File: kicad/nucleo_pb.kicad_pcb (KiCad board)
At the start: 2 copper layers, 91.4 x 91.4 mm, 273 parts, among them CN10 2X19_HEADER, CN7 2X19_HEADER, P1 CONN_2, P10 CONN_2, P11 CONN_2, P12 CONN_2, P13 CONN_2, P14 CONN_2, P15 CONN_2, P16 CONN_2, P17 CONN_2, P18 CONN_2, P19 CONN_2, P2 CONN_2, P20 CONN_2, P21 CONN_2, P22 CONN_2, P23 CONN_2, P24 CONN_2, P25 CONN_2, P26 CONN_2, P27 CONN_2, P28 CONN_2, P29 CONN_2, P3 CONN_2, P30 CONN_2, P31 CONN_2, P32 CONN_2, P33 CONN_2, P34 CONN_2, P35 CONN_2, P36 CONN_2, P37 CONN_2, P38 CONN_2, P39 CONN_2, P4 CONN_2, P40 CONN_2, P41 CONN_2, P42 CONN_2, P43 CONN_2, P44 CONN_2, P45 CONN_2, P46 CONN_2, P47 CONN_2, P48 CONN_2, P49 CONN_2, P5 CONN_2, P50 CONN_2, P51 CONN_2, P52 CONN_2, P53 CONN_2, P54 CONN_2, P55 CONN_2, P56 CONN_2, P57 CONN_2, P58 CONN_2, P59 CONN_2, P6 CONN_2, P60 CONN_2, P61 CONN_2, P62 CONN_2, P63 CONN_2, P64 CONN_2, P65 CONN_2, P66 CONN_2, P67 CONN_2, P68 CONN_2, P69 CONN_2, P7 CONN_2, P70 CONN_2, P71 CONN_2, P72 CONN_2, P73 CONN_2, P74 CONN_2, P75 CONN_2, P76 CONN_2, P77 SOIC_AREA, P8 CONN_2, P9 CONN_2, U1 TSSOP28_BREAKOUT

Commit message: added power rails
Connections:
- PROTO_1PIN pad 10: (no net) -> /5V (x2)
- PROTO_1PIN pad 10: (no net) -> /3V3 (x11)
- PROTO_1PIN pad 10: (no net) -> /GND (x8)
- PROTO_AREA pad 1: (no net) -> /5V (x2)
- PROTO_AREA pad 7: (no net) -> /5V (x2)
- PROTO_AREA pad 8: (no net) -> /5V (x2)
- PROTO_AREA pad 3: (no net) -> /3V3
- PROTO_AREA pad 4: (no net) -> /3V3
- PROTO_AREA pad 5: (no net) -> /3V3
- PROTO_AREA pad 1: (no net) -> /GND (x2)
- PROTO_AREA pad 2: (no net) -> /5V (x2)
- PROTO_AREA pad 6: (no net) -> /5V (x2)
- PROTO_AREA pad 7: (no net) -> /GND (x2)
- PROTO_AREA pad 8: (no net) -> /GND (x2)
- PROTO_AREA pad 9: (no net) -> /5V (x2)
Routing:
- net /3V3: track 10.8 -> 89.7 mm
- net /5V: track 10.8 -> 84.9 mm
- net /GND: track 69.8 -> 138.8 mm
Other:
- board text added: "CC BY 4.0 aon@umetronics.com 2015"
- board text added: "G"
- board text added: "STM32 Nucleo Prototyping Shield v1.2"
- board text removed: "CC-BY aon@umetronics.com 2015"
- board text removed: "STM32 Nucleo Prototyping Shield v1.1"

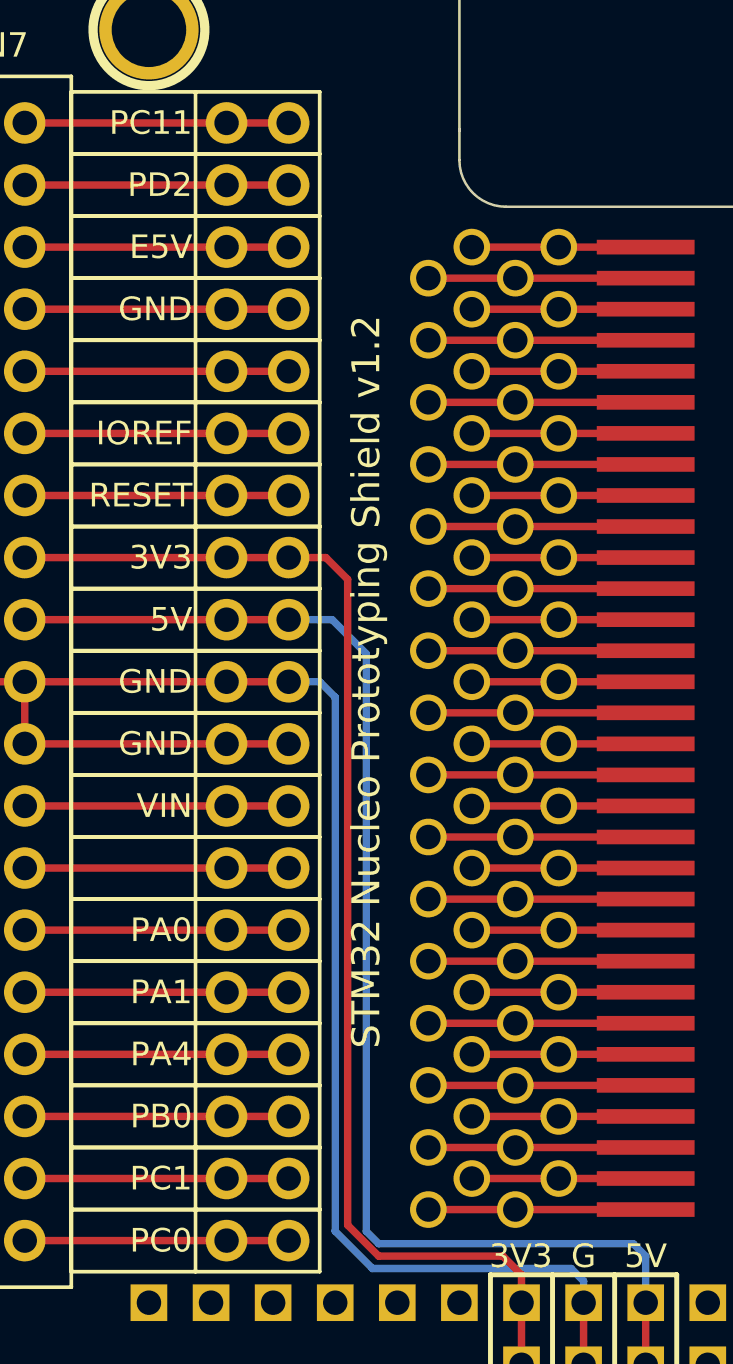
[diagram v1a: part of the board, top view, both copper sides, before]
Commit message: nucleo-64 silkscreen text
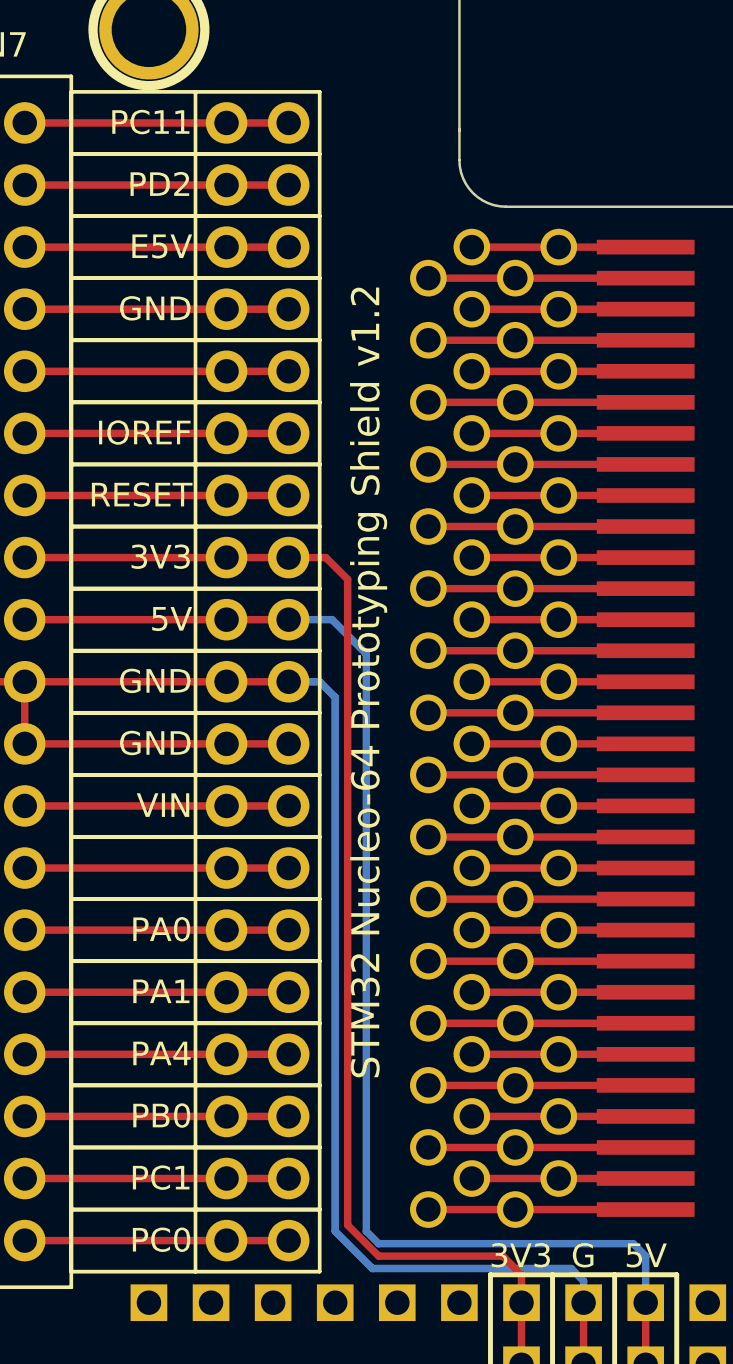
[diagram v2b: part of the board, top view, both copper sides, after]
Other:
- board text added: "STM32 Nucleo-64 Prototyping Shield v1.2"
- board text removed: "STM32 Nucleo Prototyping Shield v1.2"
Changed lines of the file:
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@@
-(kicad_pcb (version 4) (host pcbnew 4.0.0-rc1-stable)
+(kicad_pcb (version 4) (host pcbnew 4.0.0-2.201512062335+6193~38~ubuntu15.10.1-stable)
   (general
     (links 440)
     (no_connects 62)
-    (area 86.309999 50.749999 177.850001 142.290001)
+    (area 79.394029 49.6824 184.765972 142.290001)
     (thickness 1.6)
     (drawings 108)
@@
     (effects (font (size 0.9652 0.9652) (thickness 0.2032)))
   )
-  (gr_text "STM32 Nucleo Prototyping Shield v1.2" (at 116.84 80.645 90) (layer F.SilkS)
+  (gr_text "STM32 Nucleo-64 Prototyping Shield v1.2" (at 116.84 80.645 90) (layer F.SilkS)
     (effects (font (size 1.143 1.143) (thickness 0.2032)))
   )
@@
   (gr_arc (start 118.745 52.705) (end 118.745 50.8) (angle 90) (layer Edge.Cuts) (width 0.1))
   (gr_line (start 102.87 50.8) (end 114.935 50.8) (angle 90) (layer Edge.Cuts) (width 0.1))
-  (segment (start 123.19 131.445) (end 123.19 133.985) (width 0.3048) (layer F.Cu) (net 1) (status C00000))
-  (segment (start 123.19 133.985) (end 123.19 136.525) (width 0.3048) (layer F.Cu) (net 1) (status C00000))
-  (segment (start 123.19 136.525) (end 123.19 139.065) (width 0.3048) (layer F.Cu) (net 1) (status C00000))
+  (segment (start 123.19 131.445) (end 123.19 133.985) (width 0.3048) (layer F.Cu) (net 1))
+  (segment (start 123.19 133.985) (end 123.19 136.525) (width 0.3048) (layer F.Cu) (net 1))
+  (segment (start 123.19 136.525) (end 123.19 139.065) (width 0.3048) (layer F.Cu) (net 1))
   (segment (start 123.19 104.902) (end 123.19 106.045) (width 0.3048) (layer F.Cu) (net 1))
   (segment (start 122.428 104.14) (end 123.19 104.902) (width 0.3048) (layer F.Cu) (net 1))
@@
   (segment (start 111.125 62.865) (end 113.665 62.865) (width 0.3048) (layer F.Cu) (net 5))
   (segment (start 102.87 62.865) (end 111.125 62.865) (width 0.3048) (layer F.Cu) (net 5))
-  (segment (start 125.73 139.065) (end 125.73 136.525) (width 0.3048) (layer F.Cu) (net 6) (status C00000))
-  (segment (start 125.73 136.525) (end 125.73 133.985) (width 0.3048) (layer F.Cu) (net 6) (status C00000))
-  (segment (start 125.73 133.985) (end 125.73 131.445) (width 0.3048) (layer F.Cu) (net 6) (status C00000))
-  (segment (start 125.73 131.445) (end 125.73 128.905) (width 0.3048) (layer F.Cu) (net 6) (status C00000))
-  (segment (start 125.73 128.905) (end 125.73 126.365) (width 0.3048) (layer F.Cu) (net 6) (status C00000))
-  (segment (start 125.73 126.365) (end 125.73 123.825) (width 0.3048) (layer F.Cu) (net 6) (status C00000))
-  (segment (start 125.73 123.825) (end 125.73 121.285) (width 0.3048) (layer F.Cu) (net 6) (status C00000))
-  (segment (start 125.73 121.285) (end 125.73 118.745) (width 0.3048) (layer F.Cu) (net 6) (status C00000))
-  (segment (start 125.73 118.745) (end 125.73 116.205) (width 0.3048) (layer F.Cu) (net 6) (status C00000))
-  (segment (start 125.73 116.205) (end 125.73 113.665) (width 0.3048) (layer F.Cu) (net 6) (status C00000))
-  (segment (start 125.73 113.665) (end 125.73 111.125) (width 0.3048) (layer F.Cu) (net 6) (status C00000))
-  (segment (start 125.73 111.125) (end 125.73 108.585) (width 0.3048) (layer F.Cu) (net 6) (status C00000))
-  (segment (start 125.73 108.585) (end 125.73 106.045) (width 0.3048) (layer F.Cu) (net 6) (status C00000))
+  (segment (start 125.73 139.065) (end 125.73 136.525) (width 0.3048) (layer F.Cu) (net 6))
+  (segment (start 125.73 136.525) (end 125.73 133.985) (width 0.3048) (layer F.Cu) (net 6))
+  (segment (start 125.73 133.985) (end 125.73 131.445) (width 0.3048) (layer F.Cu) (net 6))
+  (segment (start 125.73 131.445) (end 125.73 128.905) (width 0.3048) (layer F.Cu) (net 6))
+  (segment (start 125.73 128.905) (end 125.73 126.365) (width 0.3048) (layer F.Cu) (net 6))
+  (segment (start 125.73 126.365) (end 125.73 123.825) (width 0.3048) (layer F.Cu) (net 6))
+  (segment (start 125.73 123.825) (end 125.73 121.285) (width 0.3048) (layer F.Cu) (net 6))
+  (segment (start 125.73 121.285) (end 125.73 118.745) (width 0.3048) (layer F.Cu) (net 6))
+  (segment (start 125.73 118.745) (end 125.73 116.205) (width 0.3048) (layer F.Cu) (net 6))
+  (segment (start 125.73 116.205) (end 125.73 113.665) (width 0.3048) (layer F.Cu) (net 6))
+  (segment (start 125.73 113.665) (end 125.73 111.125) (width 0.3048) (layer F.Cu) (net 6))
+  (segment (start 125.73 111.125) (end 125.73 108.585) (width 0.3048) (layer F.Cu) (net 6))
+  (segment (start 125.73 108.585) (end 125.73 106.045) (width 0.3048) (layer F.Cu) (net 6))
   (segment (start 113.665 80.645) (end 114.935 80.645) (width 0.3048) (layer B.Cu) (net 6))
   (segment (start 125.73 105.156) (end 125.73 106.045) (width 0.3048) (layer B.Cu) (net 6))
@@
   (segment (start 113.0808 133.096) (end 117.7648 133.096) (width 0.1524) (layer F.Cu) (net 100))
   (segment (start 112.746 133.4308) (end 113.0808 133.096) (width 0.1524) (layer F.Cu) (net 100))
-  (segment (start 128.27 106.045) (end 128.27 108.585) (width 0.3048) (layer F.Cu) (net 101) (status C00000))
-  (segment (start 128.27 108.585) (end 128.27 111.125) (width 0.3048) (layer F.Cu) (net 101) (status C00000))
-  (segment (start 128.27 111.125) (end 128.27 113.665) (width 0.3048) (layer F.Cu) (net 101) (status C00000))
-  (segment (start 128.27 113.665) (end 128.27 116.205) (width 0.3048) (layer F.Cu) (net 101) (status C00000))
-  (segment (start 128.27 116.205) (end 128.27 118.745) (width 0.3048) (layer F.Cu) (net 101) (status C00000))
-  (segment (start 128.27 118.745) (end 128.27 121.285) (width 0.3048) (layer F.Cu) (net 101) (status C00000))
-  (segment (start 128.27 121.285) (end 128.27 123.825) (width 0.3048) (layer F.Cu) (net 101) (status C00000))
-  (segment (start 128.27 123.825) (end 128.27 126.365) (width 0.3048) (layer F.Cu) (net 101) (status C00000))
-  (segment (start 128.27 126.365) (end 128.27 128.905) (width 0.3048) (layer F.Cu) (net 101) (status C00000))
-  (segment (start 128.27 128.905) (end 128.27 131.445) (width 0.3048) (layer F.Cu) (net 101) (status C00000))
-  (segment (start 128.27 131.445) (end 128.27 133.985) (width 0.3048) (layer F.Cu) (net 101) (status C00000))
-  (segment (start 128.27 133.985) (end 128.27 136.525) (width 0.3048) (layer F.Cu) (net 101) (status C00000))
-  (segment (start 128.27 136.525) (end 128.27 139.065) (width 0.3048) (layer F.Cu) (net 101) (status C00000))
+  (segment (start 128.27 106.045) (end 128.27 108.585) (width 0.3048) (layer F.Cu) (net 101))
+  (segment (start 128.27 108.585) (end 128.27 111.125) (width 0.3048) (layer F.Cu) (net 101))
+  (segment (start 128.27 111.125) (end 128.27 113.665) (width 0.3048) (layer F.Cu) (net 101))
+  (segment (start 128.27 113.665) (end 128.27 116.205) (width 0.3048) (layer F.Cu) (net 101))
+  (segment (start 128.27 116.205) (end 128.27 118.745) (width 0.3048) (layer F.Cu) (net 101))
+  (segment (start 128.27 118.745) (end 128.27 121.285) (width 0.3048) (layer F.Cu) (net 101))
+  (segment (start 128.27 121.285) (end 128.27 123.825) (width 0.3048) (layer F.Cu) (net 101))
+  (segment (start 128.27 123.825) (end 128.27 126.365) (width 0.3048) (layer F.Cu) (net 101))
+  (segment (start 128.27 126.365) (end 128.27 128.905) (width 0.3048) (layer F.Cu) (net 101))
+  (segment (start 128.27 128.905) (end 128.27 131.445) (width 0.3048) (layer F.Cu) (net 101))
+  (segment (start 128.27 131.445) (end 128.27 133.985) (width 0.3048) (layer F.Cu) (net 101))
+  (segment (start 128.27 133.985) (end 128.27 136.525) (width 0.3048) (layer F.Cu) (net 101))
+  (segment (start 128.27 136.525) (end 128.27 139.065) (width 0.3048) (layer F.Cu) (net 101))
   (segment (start 128.27 106.045) (end 128.27 104.14) (width 0.3048) (layer B.Cu) (net 101))
   (segment (start 115.443 78.105) (end 113.665 78.105) (width 0.3048) (layer B.Cu) (net 101))
